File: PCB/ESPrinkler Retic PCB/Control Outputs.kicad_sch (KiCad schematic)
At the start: 99 parts, among them Q10 AO3400A, Q11 AO3400A, Q3 AO3400A, Q4 AO3400A, Q5 AO3400A, Q6 AO3400A, Q7 AO3400A, Q8 AO3400A, Q9 AO3400A, U10 MOC3063S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

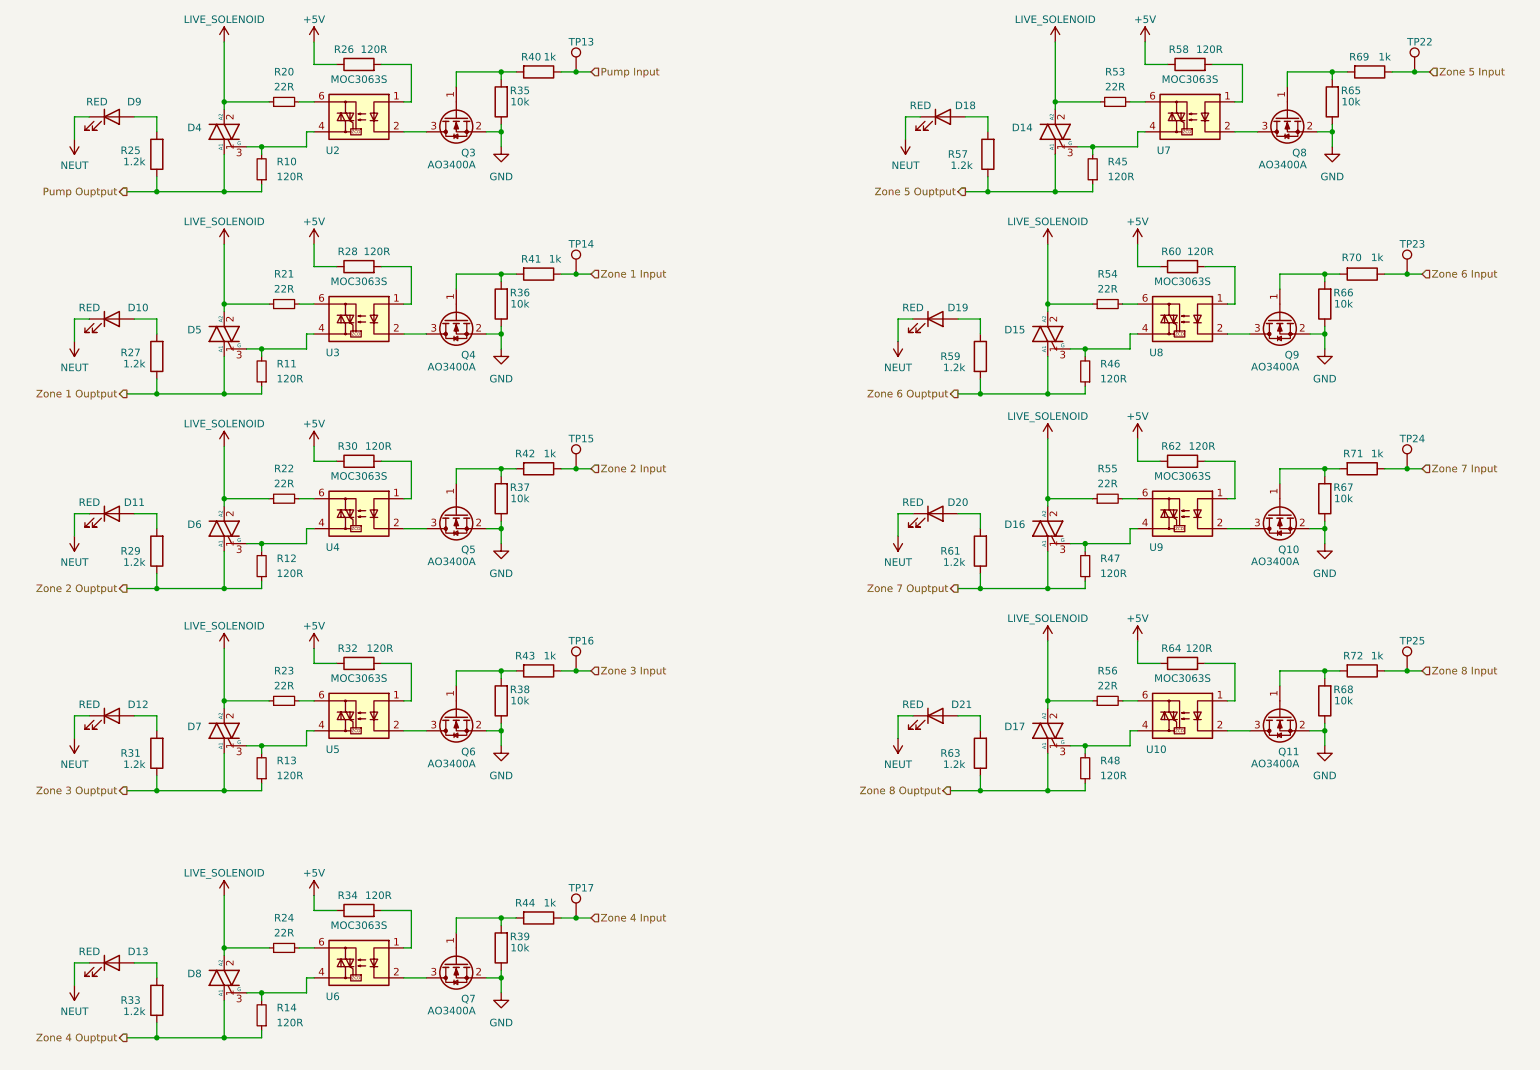
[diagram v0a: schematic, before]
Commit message: Change DC-DC converter & PCB routing
Previous DC-DC converter max input voltage was close to VIN. Changed out for 40V rated input, and a simpler design.

Also re-routed 5V rail to top layer to reduce layer swapping using vias for power lines
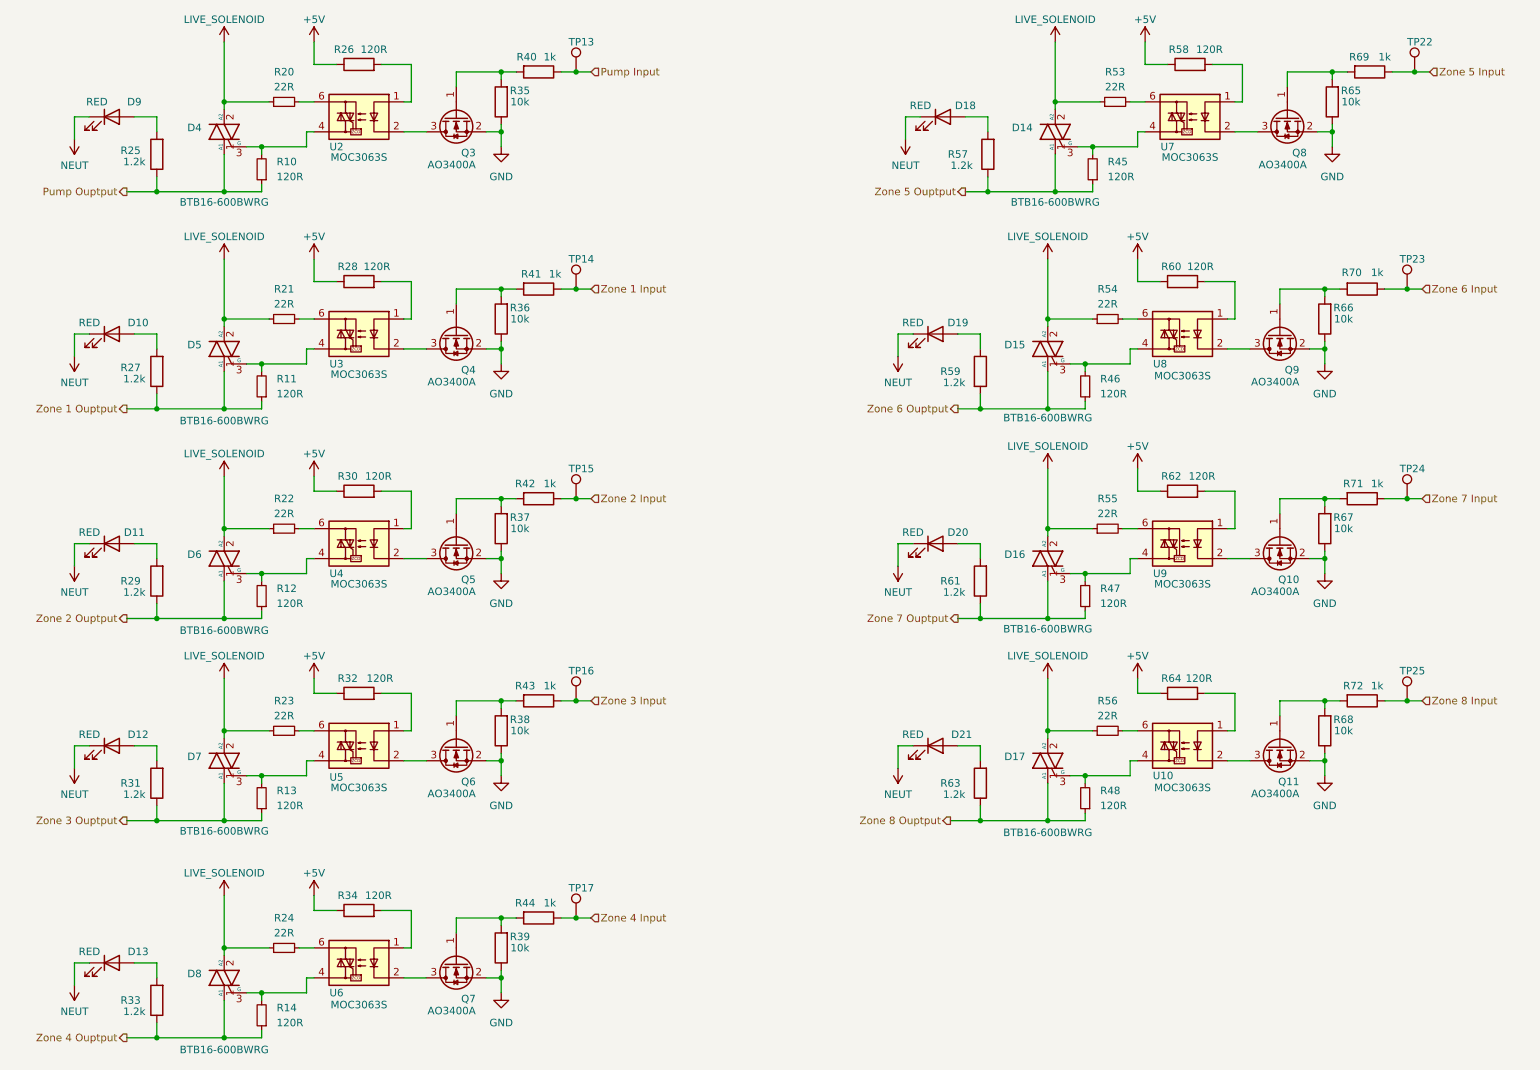
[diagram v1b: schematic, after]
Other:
- moved on the sheet: D10, D11, D12, D15, D16, D17, D19, D20, D21, D5, D6, D7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

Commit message: Labelling as V2.0
Repo needs to change, I have been using it poorly. V2.0 will be the next "main branch". After that, forks will be used instead

Also in this commit, I have updated the custom footprints and updated the links to them in the project.
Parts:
- D14, D15, D16, D17, D4, D5, D6, D7, D8: value Generic_Triac_A1A2G -> BTB16-600BWRG
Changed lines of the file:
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@@
 		(title "ESPrinkler Retic Controller")
 		(date "2025-06-01")
-		(rev "1.1")
+		(rev "2.0")
+		(comment 1 "Designed by: Slippery-Carrot")
+		(comment 3 "github.com/slippery-carrot/ESPrinkler-Retic-Controller")
 	)
 	(junction
@@
 		(dnp no)
 		(property "Reference" "D15"
-			(at 193.04 72.9614 0)
+			(at 196.342 64.516 0)
 			(show_name no)
 			(do_not_autoplace no)
@@
 			)
 		)
-		(property "Value" "Generic_Triac_A1A2G"
-			(at 193.04 75.5014 0)
-			(hide yes)
+		(property "Value" "BTB16-600BWRG"
+			(at 196.342 67.056 0)
 			(show_name no)
 			(do_not_autoplace no)
@@
 		(property "Manufacturer P/N" "BTB16-600BWRG"
 			(at 196.85 85.344 0)
+			(hide yes)
 			(show_name no)
 			(do_not_autoplace no)
@@
 		(dnp no)
 		(property "Reference" "D16"
-			(at 193.04 108.5214 0)
+			(at 196.088 100.076 0)
 			(show_name no)
 			(do_not_autoplace no)
@@
 			)
 		)
-		(property "Value" "Generic_Triac_A1A2G"
-			(at 193.04 111.0614 0)
-			(hide yes)
+		(property "Value" "BTB16-600BWRG"
+			(at 196.088 102.616 0)
 			(show_name no)
 			(do_not_autoplace no)
@@
 		(property "Manufacturer P/N" "BTB16-600BWRG"
 			(at 196.85 121.158 0)
+			(hide yes)
 			(show_name no)
 			(do_not_autoplace no)
@@
 		(dnp no)
 		(property "Reference" "D6"
-			(at 53.34 108.5214 0)
+			(at 56.896 99.822 0)
 			(show_name no)
 			(do_not_autoplace no)
@@
 			)
 		)
-		(property "Value" "Generic_Triac_A1A2G"
-			(at 53.34 111.0614 0)
-			(hide yes)
+		(property "Value" "BTB16-600BWRG"
+			(at 56.896 102.362 0)
 			(show_name no)
 			(do_not_autoplace no)
@@
 		(property "Manufacturer P/N" "BTB16-600BWRG"
 			(at 57.15 121.412 0)
+			(hide yes)
 			(show_name no)
 			(do_not_autoplace no)
@@
 		(dnp no)
 		(property "Reference" "D21"
-			(at 182.245 139.065 0)
+			(at 173.99 139.446 0)
 			(show_name no)
 			(do_not_autoplace no)
@@
 		)
 		(property "Value" "RED"
-			(at 173.99 139.065 0)
+			(at 177.8 144.018 0)
 			(show_name no)
 			(do_not_autoplace no)
@@
 		(dnp no)
 		(property "Reference" "D20"
-			(at 181.61 104.775 0)
+			(at 173.482 104.902 0)
 			(show_name no)
 			(do_not_autoplace no)
@@
 		)
 		(property "Value" "RED"
-			(at 173.99 104.775 0)
+			(at 177.8 109.982 0)
 			(show_name no)
 			(do_not_autoplace no)
@@
 		(dnp no)
 		(property "Reference" "D11"
-			(at 41.91 104.775 0)
+			(at 34.544 104.648 0)
 			(show_name no)
 			(do_not_autoplace no)
@@
 		)
 		(property "Value" "RED"
-			(at 34.29 104.775 0)
+			(at 38.354 109.728 0)
 			(show_name no)
 			(do_not_autoplace no)
@@
 		(dnp no)
 		(property "Reference" "D19"
-			(at 181.61 69.215 0)
+			(at 173.736 68.834 0)
 			(show_name no)
 			(do_not_autoplace no)
@@
 		)
 		(property "Value" "RED"
-			(at 173.99 69.215 0)
+			(at 177.8 74.168 0)
 			(show_name no)
 			(do_not_autoplace no)
@@
 		(dnp no)
 		(property "Reference" "D5"
-			(at 53.34 72.9614 0)
+			(at 56.896 64.516 0)
 			(show_name no)
 			(do_not_autoplace no)
@@
 			)
 		)
-		(property "Value" "Generic_Triac_A1A2G"
-			(at 53.34 75.5014 0)
-			(hide yes)
+		(property "Value" "BTB16-600BWRG"
+			(at 56.896 67.056 0)
 			(show_name no)
 			(do_not_autoplace no)
@@
 		(property "Manufacturer P/N" "BTB16-600BWRG"
 			(at 57.15 85.852 0)
+			(hide yes)
 			(show_name no)
 			(do_not_autoplace no)
@@
 		(dnp no)
 		(property "Reference" "D18"
-			(at 182.88 32.385 0)
+			(at 175.26 32.258 0)
 			(show_name no)
 			(do_not_autoplace no)
@@
 		)
 		(property "Value" "RED"
-			(at 175.26 32.385 0)
+			(at 179.324 37.084 0)
 			(show_name no)
 			(do_not_autoplace no)
@@
 		(dnp no)
 		(property "Reference" "D12"
-			(at 42.545 139.065 0)
+			(at 33.782 139.446 0)
 			(show_name no)
 			(do_not_autoplace no)
@@
 		)
 		(property "Value" "RED"
-			(at 34.29 139.065 0)
+			(at 38.354 143.764 0)
 			(show_name no)
 			(do_not_autoplace no)
@@
 		(dnp no)
 		(property "Reference" "D13"
-			(at 42.545 175.895 0)
+			(at 33.782 176.53 0)
 			(show_name no)
 			(do_not_autoplace no)
@@
 		)
 		(property "Value" "RED"
-			(at 34.29 175.895 0)
+			(at 38.1 180.594 0)
 			(show_name no)
 			(do_not_autoplace no)
@@
 		(dnp no)
 		(property "Reference" "D4"
-			(at 53.34 36.1314 0)
+			(at 56.642 27.432 0)
 			(show_name no)
 			(do_not_autoplace no)
@@
 			)
 		)
-		(property "Value" "Generic_Triac_A1A2G"
-			(at 53.34 38.6714 0)
-			(hide yes)
+		(property "Value" "BTB16-600BWRG"
+			(at 56.642 29.972 0)
 			(show_name no)
 			(do_not_autoplace no)
@@
 		(property "Manufacturer P/N" "BTB16-600BWRG"
 			(at 57.15 48.768 0)
+			(hide yes)
 			(show_name no)
 			(do_not_autoplace no)
@@
 		(dnp no)
 		(property "Reference" "D7"
-			(at 53.34 142.8114 0)
+			(at 56.642 134.366 0)
 			(show_name no)
 			(do_not_autoplace no)
@@
 			)
 		)
-		(property "Value" "Generic_Triac_A1A2G"
-			(at 53.34 145.3514 0)
-			(hide yes)
+		(property "Value" "BTB16-600BWRG"
+			(at 56.642 136.906 0)
 			(show_name no)
 			(do_not_autoplace no)
@@
 		(property "Manufacturer P/N" "BTB16-600BWRG"
 			(at 57.15 155.448 0)
+			(hide yes)
 			(show_name no)
 			(do_not_autoplace no)
@@
 		(dnp no)
 		(property "Reference" "D9"
-			(at 41.91 31.75 0)
+			(at 34.798 32.766 0)
 			(show_name no)
 			(do_not_autoplace no)
@@
 		)
 		(property "Value" "RED"
-			(at 35.56 31.75 0)
+			(at 38.1 37.338 0)
 			(show_name no)
 			(do_not_autoplace no)
@@
 		(dnp no)
 		(property "Reference" "D8"
-			(at 53.34 179.6414 0)
+			(at 56.388 170.942 0)
 			(show_name no)
 			(do_not_autoplace no)
@@
 			)
 		)
-		(property "Value" "Generic_Triac_A1A2G"
-			(at 53.34 182.1814 0)
-			(hide yes)
+		(property "Value" "BTB16-600BWRG"
+			(at 56.388 173.482 0)
 			(show_name no)
 			(do_not_autoplace no)
@@
 		(property "Manufacturer P/N" "BTB16-600BWRG"
 			(at 57.15 192.532 0)
+			(hide yes)
 			(show_name no)
 			(do_not_autoplace no)
@@
 		(dnp no)
 		(property "Reference" "D10"
-			(at 42.545 69.215 0)
+			(at 34.29 69.342 0)
 			(show_name no)
 			(do_not_autoplace no)
@@
 		)
 		(property "Value" "RED"
-			(at 34.29 69.215 0)
+			(at 37.846 74.422 0)
 			(show_name no)
 			(do_not_autoplace no)
@@
 		(dnp no)
 		(property "Reference" "D17"
-			(at 193.04 142.8114 0)
+			(at 196.088 134.112 0)
 			(show_name no)
 			(do_not_autoplace no)
@@
 			)
 		)
-		(property "Value" "Generic_Triac_A1A2G"
-			(at 193.04 145.3514 0)
-			(hide yes)
+		(property "Value" "BTB16-600BWRG"
+			(at 196.088 136.652 0)
 			(show_name no)
 			(do_not_autoplace no)
@@
 		(property "Manufacturer P/N" "BTB16-600BWRG"
 			(at 196.85 155.702 0)
+			(hide yes)
 			(show_name no)
 			(do_not_autoplace no)
@@
 		(dnp no)
 		(property "Reference" "D14"
-			(at 194.31 36.1314 0)
+			(at 197.612 27.178 0)
 			(show_name no)
 			(do_not_autoplace no)
@@
 			)
 		)
-		(property "Value" "Generic_Triac_A1A2G"
-			(at 194.31 38.6714 0)
-			(hide yes)
+		(property "Value" "BTB16-600BWRG"
+			(at 197.612 29.718 0)
 			(show_name no)
 			(do_not_autoplace no)
@@
 		(property "Manufacturer P/N" "BTB16-600BWRG"
 			(at 198.12 48.768 0)
+			(hide yes)
 			(show_name no)
 			(do_not_autoplace no)
